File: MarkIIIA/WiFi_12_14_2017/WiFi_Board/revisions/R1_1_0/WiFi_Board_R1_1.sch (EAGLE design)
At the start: 26 parts, among them P3 USB-B1HSB6, P4 POWER_JACKPTH, P9 44764-1201, T1 BSS138PS

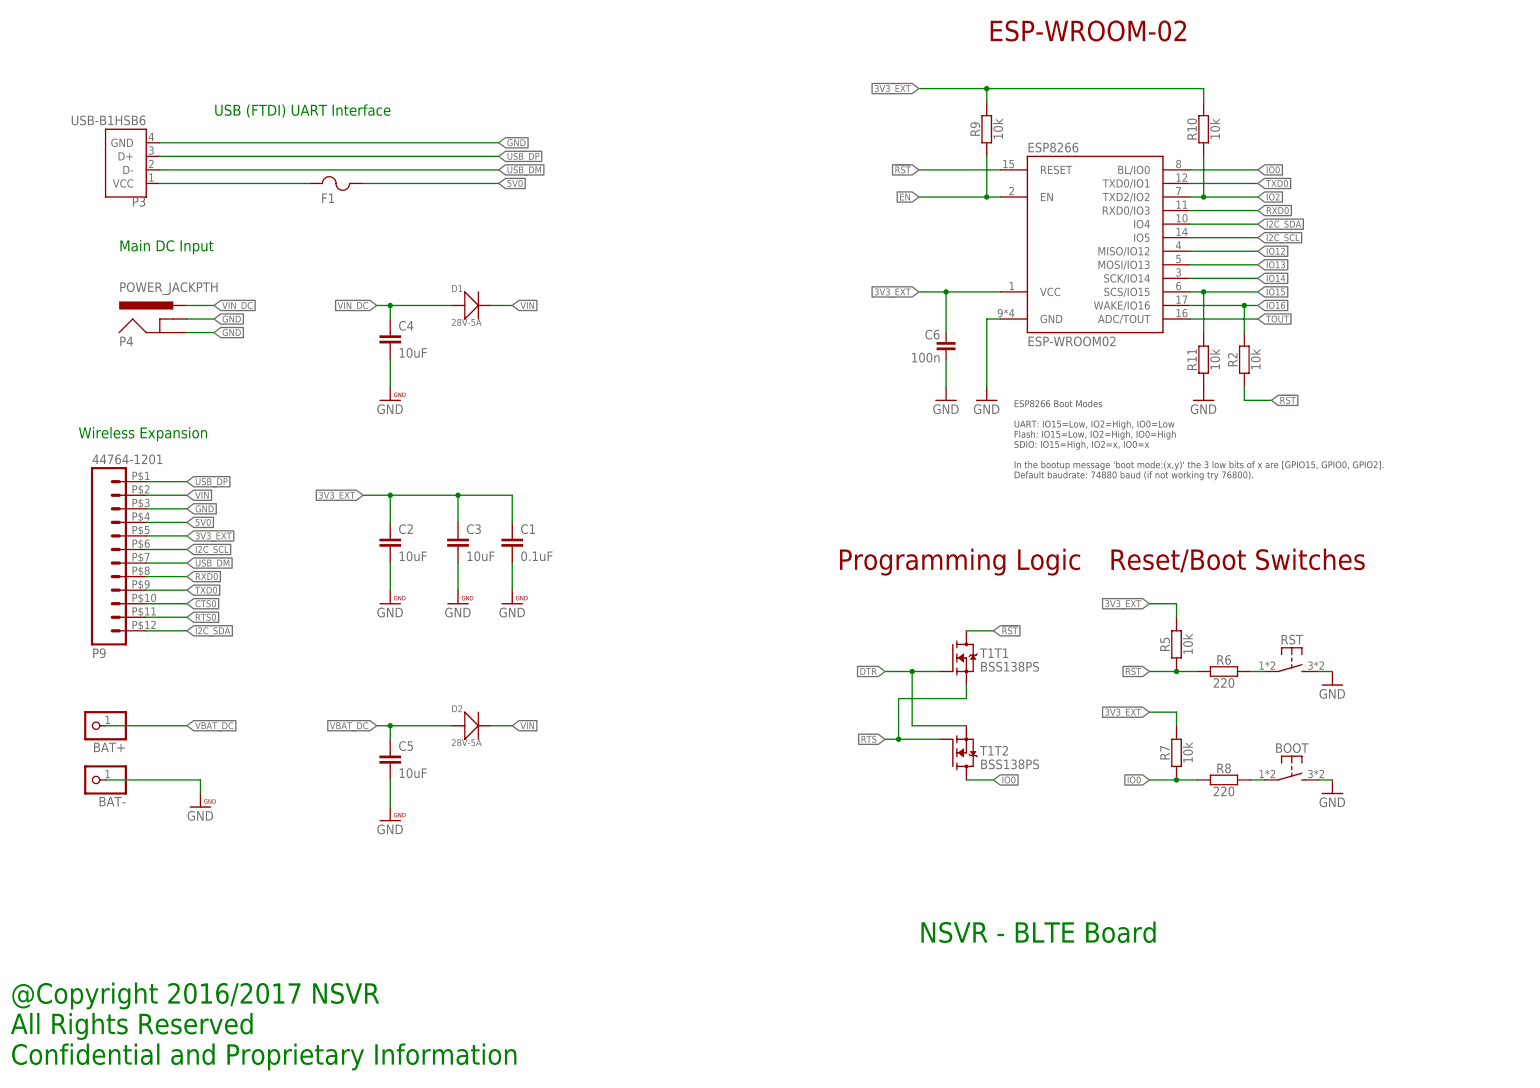
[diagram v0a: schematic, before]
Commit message: Revise WiFi Board to increase Case Clearance
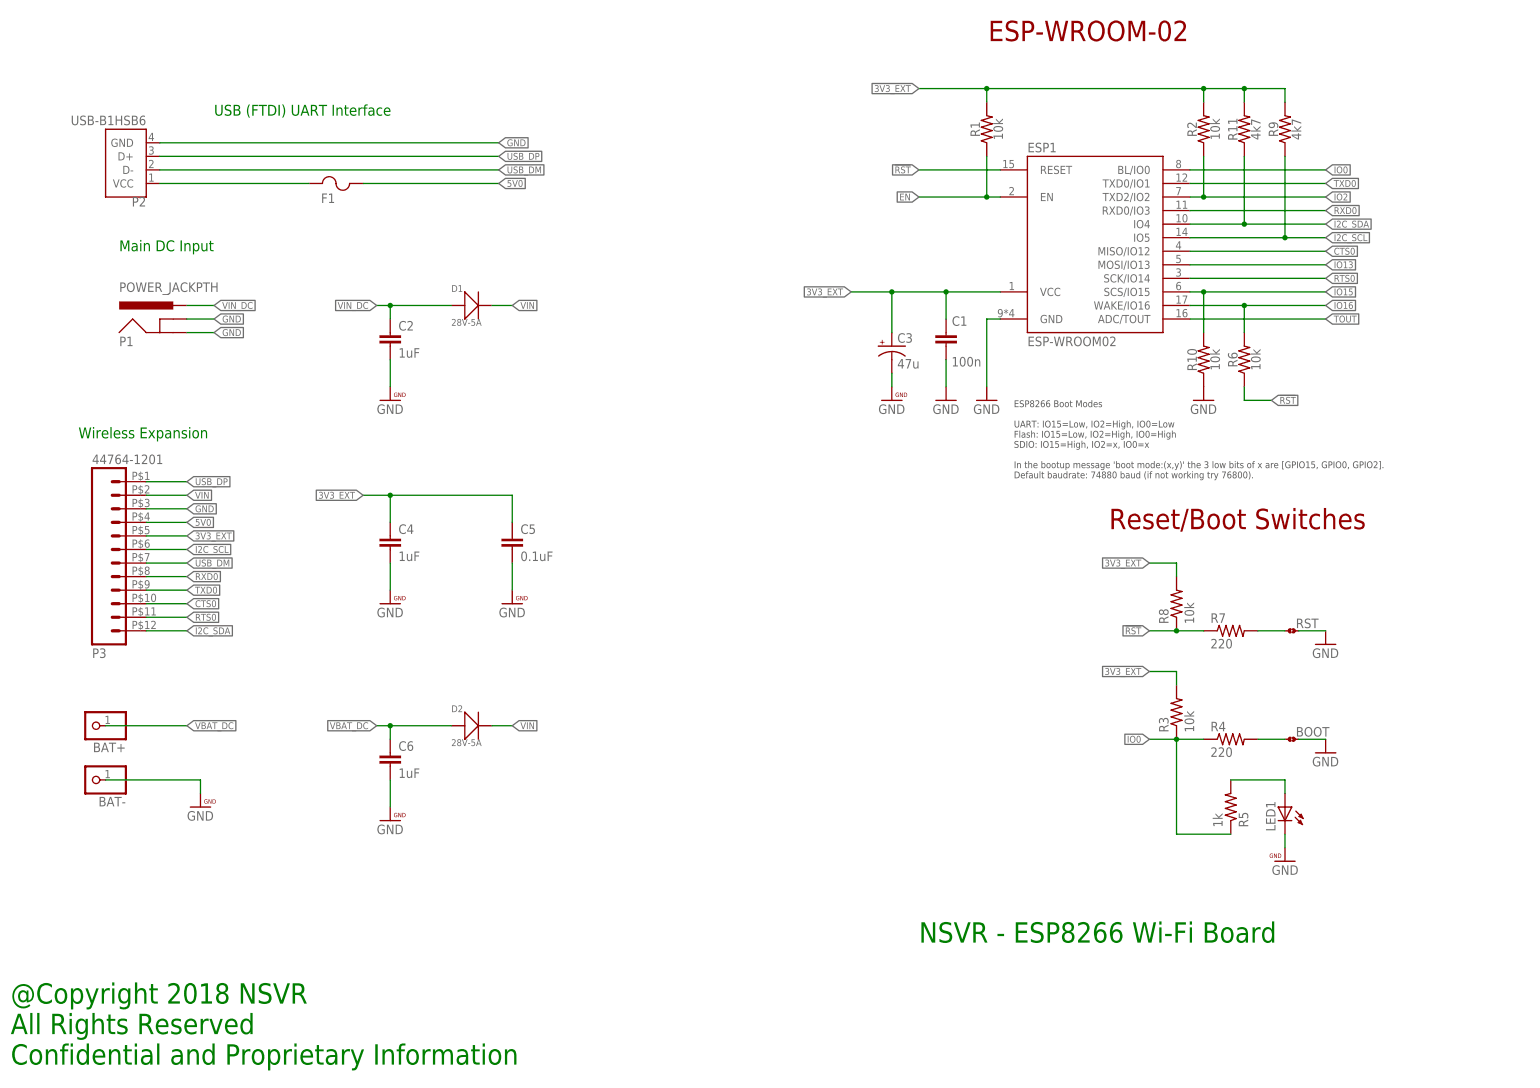
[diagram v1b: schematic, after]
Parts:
- removed P9: 44764-1201, nsvr:44764-1201
- removed T1: BSS138PS, we-transistor:BSS138PS
- added LED1: (no value), led:LEDCHIP-LED0603
- added P2: USB-B1HSB6, USB-B1HSB6:USB-B1HSB6
- added R1, R3: 10k, PatternAgents-ProtoPads:RESISTOR0402-TYP
- added R4: 220, PatternAgents-ProtoPads:RESISTOR0402-TYP
- BOOT, RST: value SW-TACTILE-PTS840P -> (none); device we-switch:SW-TACTILE-PTS840P -> PatternAgents-ProtoPads:JMP-2-NO-PTH
- C1: value 0.1uF -> 100n; device PatternAgents-ProtoPads:CAP0603-CAP -> PatternAgents-ProtoPads:CAP0402-CAP
- C2, C4: value 10uF -> 1uF; device PatternAgents-ProtoPads:CAP0603-CAP -> PatternAgents-ProtoPads:CAP0402-CAP
- C3: value 10uF -> 47u; device PatternAgents-ProtoPads:CAP0603-CAP -> SparkFun-Capacitors:CAP_POLD
- C5: value 10uF -> 0.1uF; device PatternAgents-ProtoPads:CAP0603-CAP -> PatternAgents-ProtoPads:CAP0402-CAP
- C6: value 100n -> 1uF; device we-rcl:CAPACITOR-0402 -> PatternAgents-ProtoPads:CAP0402-CAP
- P3: value USB-B1HSB6 -> 44764-1201; device USB-B1HSB6:USB-B1HSB6 -> nsvr:44764-1201
- R10, R2: device we-rcl:RESISTOR-0402 -> PatternAgents-ProtoPads:RESISTOR0402-TYP
- R11, R9: value 10k -> 4k7; device we-rcl:RESISTOR-0402 -> PatternAgents-ProtoPads:RESISTOR0402-TYP
- R5: value 10k -> 1k; device we-rcl:RESISTOR-0402 -> PatternAgents-ProtoPads:RESISTOR0402-TYP
- R6, R8: value 220 -> 10k; device we-rcl:RESISTOR-0402 -> PatternAgents-ProtoPads:RESISTOR0402-TYP
- R7: value 10k -> 220; device we-rcl:RESISTOR-0402 -> PatternAgents-ProtoPads:RESISTOR0402-TYP
- renumbered ESP8266 to ESP1, P4 to P1
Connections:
- removed net DTR: T1T1.G, T1T2.S
- removed net IO12: ESP1.MISO/IO12
- removed net IO14: ESP1.SCK/IO14
- removed net RTS: T1T1.S, T1T2.G
- new net LED1: LED1.A, R5.2
- net !RST: now also R7.1, R8.1; no longer R2.1, R5.1, T1T1.D
- net 3V3_EXT: now also C1.2, C3.+, C4.1, C5.1, P3.5, R1.2, R11.2, R2.2, R3.2, R8.2; no longer C1.1, C2.1, C3.1, C6.2, P9.5, R10.2, R5.2, R7.2
- net 5V0: now also P3.4; no longer P9.4
- net CTS0: now also ESP1.MISO/IO12, P3.10; no longer P9.10
- net EN: now also R1.1; no longer R9.1
- net GND: now also BOOT.2, C1.1, C3.-, C6.2, LED1.C, P2.GND, P3.3, R10.1, RST.2; no longer BOOT.S1, C1.2, C3.2, C6.1, P3.GND, P9.3, R11.1, RST.S1
- net I2C_SCL: now also P3.6, R9.1; no longer P9.6
- net I2C_SDA: now also P3.12, R11.1; no longer P9.12
- net IO0: now also R3.1, R4.1, R5.1; no longer R7.1, R8.1, T1T2.D
- net IO15: now also R10.2; no longer R11.2
- net IO16: now also R6.2; no longer R2.2
- net IO2: now also R2.1; no longer R10.1
- net N$1: now also R7.2, RST.1; no longer R6.2, RST.P1
- net N$2: now also BOOT.1, R4.2; no longer BOOT.P1, R8.2
- net RTS0: now also ESP1.SCK/IO14, P3.11; no longer P9.11
- net RXD0: now also P3.8; no longer P9.8
- net TXD0: now also P3.9; no longer P9.9
- net USB_DM: now also P2.D-, P3.7; no longer P3.D-, P9.7
- net USB_DP: now also P2.D+, P3.1; no longer P3.D+, P9.1
- net VBAT_DC: now also C6.1; no longer C5.1
- net VBUS_IN: now also P2.VCC; no longer P3.VCC
- net VIN: now also P3.2; no longer P9.2
- net VIN_DC: now also C2.1; no longer C4.1
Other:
- note added: "@Copyright 2018 NSVR All Rights Reserved Confidential and Proprietary Information"
- note added: "NSVR - ESP8266 Wi-Fi Board"
- note removed: "@Copyright 2016/2017 NSVR All Rights Reserved Confidential and Proprietary Information"
- note removed: "NSVR - BLTE Board"
- note removed: "Programming Logic"
- moved on the sheet: C1, C2, C4, C5
